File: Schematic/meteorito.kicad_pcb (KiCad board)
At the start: 2 copper layers, 95.3 x 89.4 mm, 12 parts, among them P1 DH22, P10 CONN_01X10, P2 GY-ML8511, P3 BMP180, P4 Hall, P5 Hall, P6 Hall, P7 CONN_01X10, P8 CONN_01X10, P9 CONN_01X10

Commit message: v0.2
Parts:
- added G***: LOGO, Aesthetics:meteorito, F.Cu at (56.5, 99.7)
- added G***: LOGO, Aesthetics:electronic_cats_logo_8x6, F.Cu at (65.4, 66.5)
- added G***: LOGO, Aesthetics:hacedores, B.Cu at (125.3, 116.7)
- added G***: LOGO, Aesthetics:redmet, B.Cu at (50.3, 122.3)
- added svg2mod: electronic, Aesthetics:titule_electronic_med, B.Cu at (89.5, 104.4)
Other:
- board text added: "Con ayuda de:"
- board text added: "v0.2"
- board text removed: "Con apoyo de:"
- board text removed: "v0.1"

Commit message: Review
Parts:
- moved P3 30.4 mm to (119.4, 126.7), turned to 180 degrees
- moved P2 7.17 mm to (119.6, 131.5), turned to 270 degrees
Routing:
- net +5V: track 112.3 -> 166.4 mm
- net /IO21: track 44.3 -> 60.9 mm
- net +3V3: track 104.2 -> 95.7 mm
- net /IO33: track 46.2 -> 40.8 mm
- net /IO22: track 59.7 -> 64.8 mm

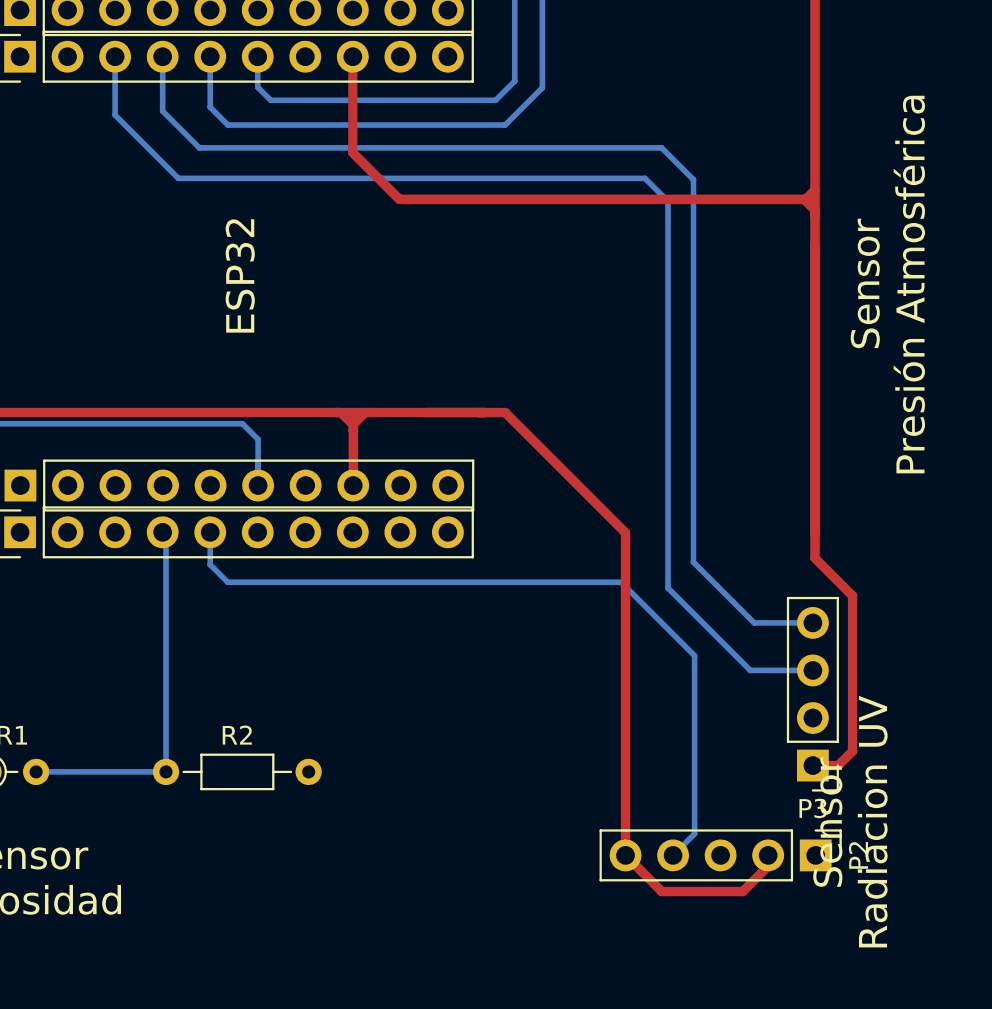
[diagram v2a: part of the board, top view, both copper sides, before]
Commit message: Change in  track
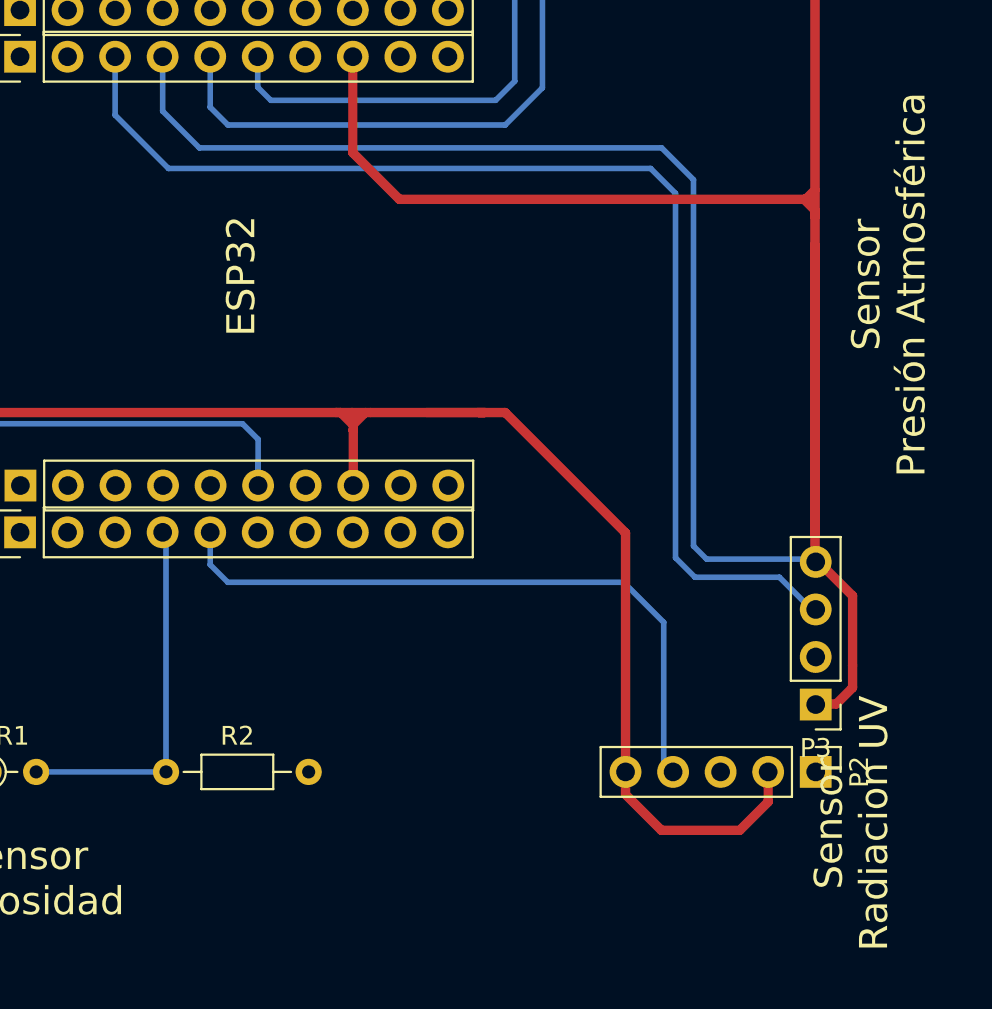
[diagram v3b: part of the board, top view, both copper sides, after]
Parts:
- moved P2 4.46 mm to (119.6, 127.0)
- moved P3 3.26 mm to (119.6, 123.4)
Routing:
- net /IO33: track 40.8 -> 35.4 mm
- net +5V: track 166.4 -> 163.2 mm
- net +3V3: track 95.7 -> 93.5 mm
- net /IO22: track 64.8 -> 62.6 mm
- net /IO21: track 60.9 -> 59.0 mm
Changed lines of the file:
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@@
     (thickness 1.6)
     (drawings 36)
-    (tracks 130)
+    (tracks 132)
     (zones 0)
     (modules 17)
@@
   )
   (module Connector_PinHeader_2.54mm:PinHeader_1x04_P2.54mm_Vertical (layer F.Cu)
-    (at 119.44 126.66 180)
+    (at 119.59 123.4 180)
     (descr "Through hole straight pin header, 1x04, 2.54mm pitch, single row")
     (tags "Through hole pin header THT 1x04 2.54mm single row")
@@
   )
   (module Connector_PinHeader_2.54mm:PinHeader_1x05_P2.54mm_Vertical (layer F.Cu)
-    (at 119.59 131.46 270)
+    (at 119.59 127 270)
     (descr "Through hole straight pin header, 1x05, 2.54mm pitch, single row")
     (tags "Through hole pin header THT 1x05 2.54mm single row")
@@
   (segment (start 119.55 114.29) (end 119.55 115.58) (width 0.5) (layer F.Cu) (net 2))
   (segment (start 119.55 115.58) (end 121.56 117.59) (width 0.5) (layer F.Cu) (net 2))
-  (segment (start 120.79 126.66) (end 119.44 126.66) (width 0.5) (layer F.Cu) (net 2))
-  (segment (start 121.56 125.89) (end 120.79 126.66) (width 0.5) (layer F.Cu) (net 2))
-  (segment (start 121.56 117.59) (end 121.56 125.89) (width 0.5) (layer F.Cu) (net 2))
-  (segment (start 82.16 91.91) (end 85.54 95.29) (width 0.3) (layer B.Cu) (net 5))
+  (segment (start 121.56 122.5) (end 121.56 121.31) (width 0.5) (layer F.Cu) (net 2))
+  (segment (start 120.69 123.37) (end 121.56 122.5) (width 0.5) (layer F.Cu) (net 2))
+  (segment (start 119.34 123.37) (end 120.69 123.37) (width 0.5) (layer F.Cu) (net 2))
+  (segment (start 121.56 117.59) (end 121.56 121.31) (width 0.5) (layer F.Cu) (net 2))
+  (segment (start 117.65 116.6) (end 119.34 118.29) (width 0.3) (layer B.Cu) (net 5))
+  (segment (start 113.14 116.6) (end 117.65 116.6) (width 0.3) (layer B.Cu) (net 5))
+  (segment (start 82.16 91.91) (end 85.01 94.76) (width 0.3) (layer B.Cu) (net 5))
+  (segment (start 85.01 94.76) (end 110.77 94.76) (width 0.3) (layer B.Cu) (net 5))
+  (segment (start 110.77 94.76) (end 112.1 96.09) (width 0.3) (layer B.Cu) (net 5))
+  (segment (start 112.1 96.09) (end 112.1 115.56) (width 0.3) (layer B.Cu) (net 5))
   (segment (start 82.16 88.79) (end 82.16 91.91) (width 0.3) (layer B.Cu) (net 5))
-  (segment (start 85.54 95.29) (end 110.47 95.29) (width 0.3) (layer B.Cu) (net 5))
-  (segment (start 110.47 95.29) (end 111.7 96.52) (width 0.3) (layer B.Cu) (net 5))
-  (segment (start 116.1 121.58) (end 119.44 121.58) (width 0.3) (layer B.Cu) (net 5))
-  (segment (start 111.7 96.52) (end 111.7 117.18) (width 0.3) (layer B.Cu) (net 5))
-  (segment (start 111.7 117.18) (end 116.1 121.58) (width 0.3) (layer B.Cu) (net 5))
-  (segment (start 116.3 119.04) (end 119.44 119.04) (width 0.3) (layer B.Cu) (net 6))
-  (segment (start 84.7 91.7) (end 86.66 93.66) (width 0.3) (layer B.Cu) (net 6))
+  (segment (start 112.1 115.56) (end 113.14 116.6) (width 0.3) (layer B.Cu) (net 5))
+  (segment (start 119.22 115.63) (end 119.34 115.75) (width 0.3) (layer B.Cu) (net 6))
+  (segment (start 113.76 115.63) (end 119.22 115.63) (width 0.3) (layer B.Cu) (net 6))
   (segment (start 84.7 88.79) (end 84.7 91.7) (width 0.3) (layer B.Cu) (net 6))
   (segment (start 86.66 93.66) (end 111.36 93.66) (width 0.3) (layer B.Cu) (net 6))
   (segment (start 111.36 93.66) (end 113.06 95.36) (width 0.3) (layer B.Cu) (net 6))
-  (segment (start 113.06 95.36) (end 113.06 115.8) (width 0.3) (layer B.Cu) (net 6))
-  (segment (start 113.06 115.8) (end 116.3 119.04) (width 0.3) (layer B.Cu) (net 6))
+  (segment (start 84.7 91.7) (end 86.66 93.66) (width 0.3) (layer B.Cu) (net 6))
+  (segment (start 113.06 95.36) (end 113.06 114.93) (width 0.3) (layer B.Cu) (net 6))
+  (segment (start 113.06 114.93) (end 113.76 115.63) (width 0.3) (layer B.Cu) (net 6))
   (segment (start 82.16 84.17) (end 82.16 86.3) (width 0.3) (layer B.Cu) (net 7))
   (segment (start 81.44 83.45) (end 82.16 84.17) (width 0.3) (layer B.Cu) (net 7))
@@
   (segment (start 89.78 90.42) (end 89.78 88.79) (width 0.3) (layer B.Cu) (net 9))
   (segment (start 90.48 91.12) (end 89.78 90.42) (width 0.3) (layer B.Cu) (net 9))
-  (segment (start 87.24 115.93) (end 87.24 114.2) (width 0.3) (layer B.Cu) (net 32))
-  (segment (start 88.18 116.87) (end 87.24 115.93) (width 0.3) (layer B.Cu) (net 32))
-  (segment (start 109.2 116.87) (end 88.18 116.87) (width 0.3) (layer B.Cu) (net 32))
-  (segment (start 113.12 120.79) (end 109.2 116.87) (width 0.3) (layer B.Cu) (net 32))
-  (segment (start 111.97 131.46) (end 113.12 130.31) (width 0.3) (layer B.Cu) (net 32))
-  (segment (start 113.12 130.31) (end 113.12 120.79) (width 0.3) (layer B.Cu) (net 32))
+  (segment (start 111.47 126.5) (end 111.97 127) (width 0.3) (layer B.Cu) (net 32))
+  (segment (start 111.47 119.01) (end 111.47 126.5) (width 0.3) (layer B.Cu) (net 32))
+  (segment (start 109.33 116.87) (end 111.47 119.01) (width 0.3) (layer B.Cu) (net 32))
+  (segment (start 88.18 116.87) (end 109.33 116.87) (width 0.3) (layer B.Cu) (net 32))
+  (segment (start 87.24 114.2) (end 87.24 115.93) (width 0.3) (layer B.Cu) (net 32))
+  (segment (start 87.24 115.93) (end 88.18 116.87) (width 0.3) (layer B.Cu) (net 32))
   (segment (start 77.94 127) (end 84.88 127) (width 0.3) (layer B.Cu) (net 33))
   (segment (start 84.88 114.38) (end 84.7 114.2) (width 0.3) (layer B.Cu) (net 33))
@@
   (segment (start 95.82 107.8) (end 101.56 107.8) (width 0.5) (layer F.Cu) (net 35))
   (segment (start 101.56 107.8) (end 101.93 107.8) (width 0.5) (layer F.Cu) (net 35))
-  (segment (start 102.31 107.8) (end 103 107.8) (width 0.5) (layer F.Cu) (net 35))
-  (segment (start 102.31 107.8) (end 101.56 107.8) (width 0.5) (layer F.Cu) (net 35))
-  (segment (start 109.43 114.23) (end 109.43 131.46) (width 0.5) (layer F.Cu) (net 35))
+  (segment (start 109.43 114.23) (end 109.43 127) (width 0.5) (layer F.Cu) (net 35))
+  (segment (start 101.56 107.8) (end 103 107.8) (width 0.5) (layer F.Cu) (net 35))
   (segment (start 103 107.8) (end 109.43 114.23) (width 0.5) (layer F.Cu) (net 35))
-  (segment (start 110.279999 132.309999) (end 109.43 131.46) (width 0.5) (layer F.Cu) (net 35))
-  (segment (start 111.36 133.39) (end 110.279999 132.309999) (width 0.5) (layer F.Cu) (net 35))
-  (segment (start 115.69 133.39) (end 111.36 133.39) (width 0.5) (layer F.Cu) (net 35))
-  (segment (start 117.05 131.46) (end 117.05 132.03) (width 0.5) (layer F.Cu) (net 35))
-  (segment (start 117.05 132.03) (end 115.69 133.39) (width 0.5) (layer F.Cu) (net 35))
+  (segment (start 109.43 128.202081) (end 111.347919 130.12) (width 0.5) (layer F.Cu) (net 35))
+  (segment (start 109.43 127) (end 109.43 128.202081) (width 0.5) (layer F.Cu) (net 35))
+  (segment (start 111.347919 130.12) (end 115.53 130.12) (width 0.5) (layer F.Cu) (net 35))
+  (segment (start 117.05 128.6) (end 117.05 127) (width 0.5) (layer F.Cu) (net 35))
+  (segment (start 115.53 130.12) (end 117.05 128.6) (width 0.5) (layer F.Cu) (net 35))
   (zone (net 3) (net_name GND) (layer F.Cu) (hatch edge 0.508)
     (connect_pads (clearance 0.508))
     (min_thickness 0.254)
-    (fill yes (arc_segments 16) (thermal_gap 0.508) (thermal_bridge_width 0.508))
+    (fill (arc_segments 16) (thermal_gap 0.508) (thermal_bridge_width 0.508))
     (polygon
       (pts
@@
     (connect_pads (clearance 0.508))
     (min_thickness 0.254)
-    (fill yes (arc_segments 16) (thermal_gap 0.508) (thermal_bridge_width 0.508))
+    (fill (arc_segments 16) (thermal_gap 0.508) (thermal_bridge_width 0.508))
     (polygon
       (pts

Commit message: fix pines
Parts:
- moved P2 6.25 mm to (113.3, 126.9)
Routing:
- net /IO33: track 35.4 -> 26.9 mm
- net +3V3: track 93.5 -> 92.2 mm
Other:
- board text added: "v1.3"
- board text removed: "v0.2"
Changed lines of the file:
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@@
-(kicad_pcb (version 20171130) (host pcbnew "(5.1.4)-1")
+(kicad_pcb (version 20171130) (host pcbnew "(5.1.5-0-10_14)")
   (general
     (thickness 1.6)
     (drawings 36)
-    (tracks 132)
+    (tracks 133)
     (zones 0)
     (modules 17)
@@
     (35 F.Paste user)
     (36 B.SilkS user)
-    (37 F.SilkS user hide)
+    (37 F.SilkS user)
     (38 B.Mask user)
     (39 F.Mask user)
@@
   )
   (module Connector_PinHeader_2.54mm:PinHeader_1x05_P2.54mm_Vertical (layer F.Cu)
-    (at 119.59 127 270)
+    (at 113.34 126.94 270)
     (descr "Through hole straight pin header, 1x05, 2.54mm pitch, single row")
     (tags "Through hole pin header THT 1x05 2.54mm single row")
@@
     (arrow2b (pts (xy 135.044286 152.50246) (xy 133.919015 153.091244)))
   )
-  (gr_text v0.2 (at 66.65 96.6 90) (layer F.SilkS)
+  (gr_text v1.3 (at 66.65 96.6 90) (layer F.SilkS)
     (effects (font (size 1.5 1.5) (thickness 0.3)))
   )
@@
     (effects (font (size 1.5 1.5) (thickness 0.3)))
   )
-  (gr_text "Sensor \nPresión Atmosférica\n" (at 123.5 100.97 90) (layer F.SilkS)
+  (gr_text "Sensor \nPresión Atmosférica\n" (at 124.81 118.62 90) (layer F.SilkS)
     (effects (font (size 1.5 1.5) (thickness 0.3)))
   )
-  (gr_text "Sensor \nRadiacion UV" (at 121.5 129.75 90) (layer F.SilkS)
+  (gr_text "Sensor \nRadiacion UV" (at 108.99 132.41) (layer F.SilkS)
     (effects (font (size 1.5 1.5) (thickness 0.3)))
   )
@@
   (segment (start 89.78 90.42) (end 89.78 88.79) (width 0.3) (layer B.Cu) (net 9))
   (segment (start 90.48 91.12) (end 89.78 90.42) (width 0.3) (layer B.Cu) (net 9))
-  (segment (start 111.47 126.5) (end 111.97 127) (width 0.3) (layer B.Cu) (net 32))
-  (segment (start 111.47 119.01) (end 111.47 126.5) (width 0.3) (layer B.Cu) (net 32))
-  (segment (start 109.33 116.87) (end 111.47 119.01) (width 0.3) (layer B.Cu) (net 32))
-  (segment (start 88.18 116.87) (end 109.33 116.87) (width 0.3) (layer B.Cu) (net 32))
   (segment (start 87.24 114.2) (end 87.24 115.93) (width 0.3) (layer B.Cu) (net 32))
   (segment (start 87.24 115.93) (end 88.18 116.87) (width 0.3) (layer B.Cu) (net 32))
+  (segment (start 88.18 116.87) (end 99.22 116.87) (width 0.3) (layer B.Cu) (net 32))
+  (segment (start 105.72 123.37) (end 105.72 126.94) (width 0.3) (layer B.Cu) (net 32))
+  (segment (start 99.22 116.87) (end 105.72 123.37) (width 0.3) (layer B.Cu) (net 32))
   (segment (start 77.94 127) (end 84.88 127) (width 0.3) (layer B.Cu) (net 33))
   (segment (start 84.88 114.38) (end 84.7 114.2) (width 0.3) (layer B.Cu) (net 33))
@@
   (segment (start 95.82 107.8) (end 101.56 107.8) (width 0.5) (layer F.Cu) (net 35))
   (segment (start 101.56 107.8) (end 101.93 107.8) (width 0.5) (layer F.Cu) (net 35))
-  (segment (start 109.43 114.23) (end 109.43 127) (width 0.5) (layer F.Cu) (net 35))
   (segment (start 101.56 107.8) (end 103 107.8) (width 0.5) (layer F.Cu) (net 35))
-  (segment (start 103 107.8) (end 109.43 114.23) (width 0.5) (layer F.Cu) (net 35))
-  (segment (start 109.43 128.202081) (end 111.347919 130.12) (width 0.5) (layer F.Cu) (net 35))
-  (segment (start 109.43 127) (end 109.43 128.202081) (width 0.5) (layer F.Cu) (net 35))
-  (segment (start 111.347919 130.12) (end 115.53 130.12) (width 0.5) (layer F.Cu) (net 35))
-  (segment (start 117.05 128.6) (end 117.05 127) (width 0.5) (layer F.Cu) (net 35))
-  (segment (start 115.53 130.12) (end 117.05 128.6) (width 0.5) (layer F.Cu) (net 35))
+  (segment (start 103 107.8) (end 105.84 110.64) (width 0.5) (layer F.Cu) (net 35))
+  (segment (start 105.84 110.64) (end 105.84 119.59) (width 0.5) (layer F.Cu) (net 35))
+  (segment (start 105.84 119.59) (end 103.18 122.25) (width 0.5) (layer F.Cu) (net 35))
+  (segment (start 103.18 122.25) (end 103.18 126.94) (width 0.5) (layer F.Cu) (net 35))
+  (segment (start 103.18 128.142081) (end 104.087919 129.05) (width 0.5) (layer B.Cu) (net 35))
+  (segment (start 103.18 126.94) (end 103.18 128.142081) (width 0.5) (layer B.Cu) (net 35))
+  (segment (start 104.087919 129.05) (end 110.27 129.05) (width 0.5) (layer B.Cu) (net 35))
+  (segment (start 110.8 128.52) (end 110.8 126.94) (width 0.5) (layer B.Cu) (net 35))
+  (segment (start 110.27 129.05) (end 110.8 128.52) (width 0.5) (layer B.Cu) (net 35))
   (zone (net 3) (net_name GND) (layer F.Cu) (hatch edge 0.508)
     (connect_pads (clearance 0.508))
     (min_thickness 0.254)
-    (fill (arc_segments 16) (thermal_gap 0.508) (thermal_bridge_width 0.508))
+    (fill yes (arc_segments 16) (thermal_gap 0.508) (thermal_bridge_width 0.508))
     (polygon
       (pts
@@
     (connect_pads (clearance 0.508))
     (min_thickness 0.254)
-    (fill (arc_segments 16) (thermal_gap 0.508) (thermal_bridge_width 0.508))
+    (fill yes (arc_segments 16) (thermal_gap 0.508) (thermal_bridge_width 0.508))
     (polygon
       (pts
